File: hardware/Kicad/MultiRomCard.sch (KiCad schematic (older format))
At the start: 9 parts, among them P1 VC4000_Cartridge_Bus, U1 Arduino_UNO, U2 74HC595, U3 74HC595, U4 74HC595, U5 6264, U6 74HC245, U7 74HC245, U8 74HC245

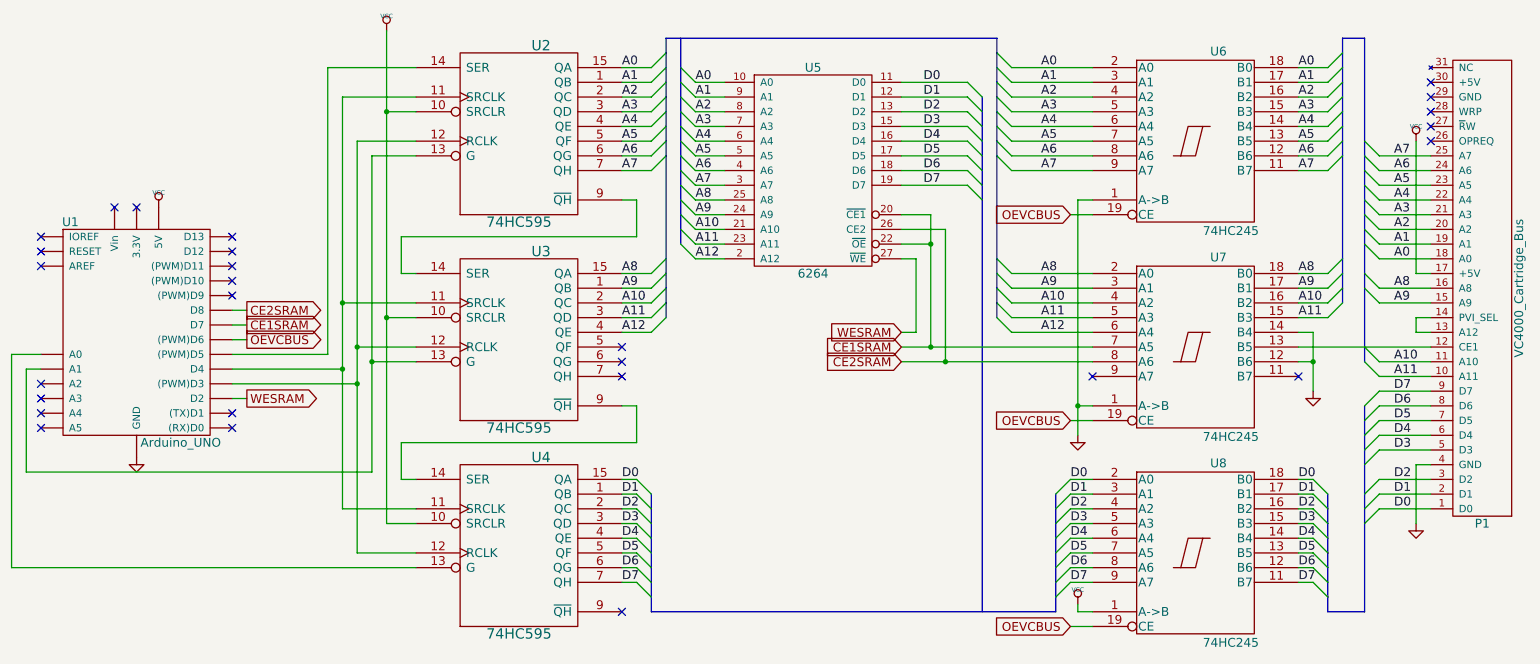
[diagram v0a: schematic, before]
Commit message: Small cosmetic changes in schematic
- Account for changes in Kicad symbol libraries that affected power
  symbols GND and VCC.
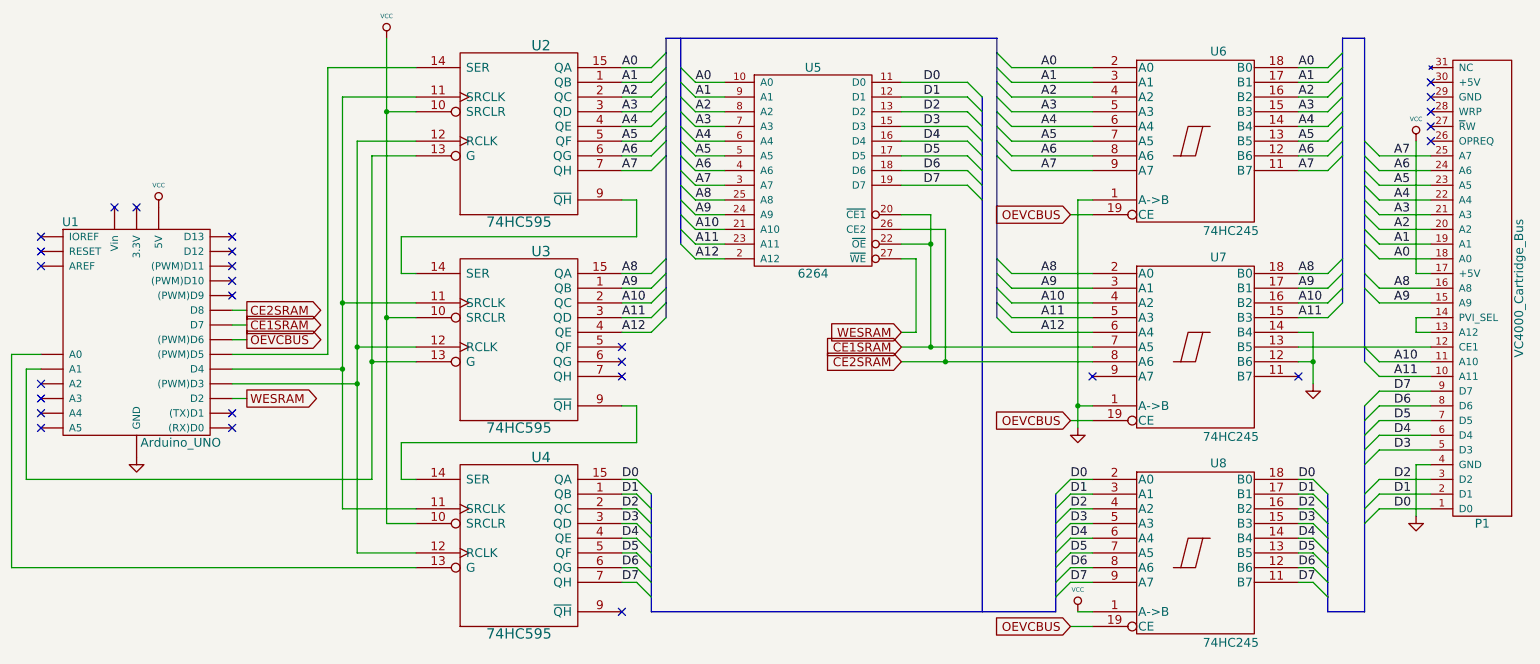
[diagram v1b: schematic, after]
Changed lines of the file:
@@
 P 10250 2350
 F 0 "#PWR7" H 10250 2450 30  0001 C CNN
-F 1 "VCC" H 10250 2450 30  0000 C CNN
+F 1 "VCC" H 10250 2500 30  0000 C CNN
 F 2 "" H 10250 2350 60  0000 C CNN
 F 3 "" H 10250 2350 60  0000 C CNN
@@
 P 1700 2800
 F 0 "#PWR2" H 1700 2900 30  0001 C CNN
-F 1 "VCC" H 1700 2900 30  0000 C CNN
+F 1 "VCC" H 1700 2950 30  0000 C CNN
 F 2 "" H 1700 2800 60  0000 C CNN
 F 3 "" H 1700 2800 60  0000 C CNN
@@
 	1    0    0    -1
 $EndComp
-$Comp
-L GND #PWR1
-U 1 1 54D739DD
-P 1550 4500
-F 0 "#PWR1" H 1550 4500 30  0001 C CNN
-F 1 "GND" H 1550 4430 30  0001 C CNN
-F 2 "" H 1550 4500 60  0000 C CNN
-F 3 "" H 1550 4500 60  0000 C CNN
-	1    1550 4500
-	1    0    0    -1
-$EndComp
 Wire Wire Line
 	4950 3000 3350 3000
@@
 	800  3900 900  3900
 Wire Wire Line
-	3150 4600 800  4600
+	3150 4650 800  4650
 Wire Wire Line
 	3150 2450 3150 3850
 Wire Wire Line
-	3150 3850 3150 4600
+	3150 3850 3150 4650
 Wire Wire Line
 	3150 3850 3450 3850
@@
 Connection ~ 3150 3850
 Wire Wire Line
-	800  4600 800  3900
+	800  4650 800  3900
 Wire Wire Line
 	2950 3900 2200 3900
@@
 L VCC #PWR3
 U 1 1 54DB48BB
-P 3250 1600
-F 0 "#PWR3" H 3250 1700 30  0001 C CNN
-F 1 "VCC" H 3250 1700 30  0000 C CNN
-F 2 "" H 3250 1600 60  0000 C CNN
-F 3 "" H 3250 1600 60  0000 C CNN
-	1    3250 1600
-	1    0    0    -1
-$EndComp
-Wire Wire Line
-	3250 1600 3250 2150
+P 3250 1650
+F 0 "#PWR3" H 3250 1750 30  0001 C CNN
+F 1 "VCC" H 3250 1800 30  0000 C CNN
+F 2 "" H 3250 1650 60  0000 C CNN
+F 3 "" H 3250 1650 60  0000 C CNN
+	1    3250 1650
+	1    0    0    -1
+$EndComp
+Wire Wire Line
+	3250 1650 3250 2150
 Wire Wire Line
 	3250 2150 3250 3550
@@
 L GND #PWR5
 U 1 1 54DB55F6
-P 7950 4350
-F 0 "#PWR5" H 7950 4350 30  0001 C CNN
-F 1 "GND" H 7950 4280 30  0001 C CNN
-F 2 "" H 7950 4350 60  0000 C CNN
-F 3 "" H 7950 4350 60  0000 C CNN
-	1    7950 4350
+P 7950 4300
+F 0 "#PWR5" H 7950 4300 30  0001 C CNN
+F 1 "GND" H 7950 4230 30  0001 C CNN
+F 2 "" H 7950 4300 60  0000 C CNN
+F 3 "" H 7950 4300 60  0000 C CNN
+	1    7950 4300
 	1    0    0    -1
 $EndComp
@@
 L VCC #PWR4
 U 1 1 54DB5800
-P 7950 5500
-F 0 "#PWR4" H 7950 5600 30  0001 C CNN
-F 1 "VCC" H 7950 5600 30  0000 C CNN
-F 2 "" H 7950 5500 60  0000 C CNN
-F 3 "" H 7950 5500 60  0000 C CNN
-	1    7950 5500
+P 7950 5550
+F 0 "#PWR4" H 7950 5650 30  0001 C CNN
+F 1 "VCC" H 7950 5700 30  0000 C CNN
+F 2 "" H 7950 5550 60  0000 C CNN
+F 3 "" H 7950 5550 60  0000 C CNN
+	1    7950 5550
 	1    0    0    -1
 $EndComp
@@
 L GND #PWR8
 U 1 1 54DB7B7A
-P 10250 4950
-F 0 "#PWR8" H 10250 4950 30  0001 C CNN
-F 1 "GND" H 10250 4880 30  0001 C CNN
-F 2 "" H 10250 4950 60  0000 C CNN
-F 3 "" H 10250 4950 60  0000 C CNN
-	1    10250 4950
-	1    0    0    -1
-$EndComp
-Wire Wire Line
-	10250 4950 10250 4550
+P 10250 4900
+F 0 "#PWR8" H 10250 4900 30  0001 C CNN
+F 1 "GND" H 10250 4830 30  0001 C CNN
+F 2 "" H 10250 4900 60  0000 C CNN
+F 3 "" H 10250 4900 60  0000 C CNN
+	1    10250 4900
+	1    0    0    -1
+$EndComp
+Wire Wire Line
+	10250 4900 10250 4550
 Wire Wire Line
 	10250 4550 10350 4550
@@
 L GND #PWR6
 U 1 1 54DB8BDD
-P 9550 4050
-F 0 "#PWR6" H 9550 4050 30  0001 C CNN
-F 1 "GND" H 9550 3980 30  0001 C CNN
-F 2 "" H 9550 4050 60  0000 C CNN
-F 3 "" H 9550 4050 60  0000 C CNN
-	1    9550 4050
+P 9550 4000
+F 0 "#PWR6" H 9550 4000 30  0001 C CNN
+F 1 "GND" H 9550 3930 30  0001 C CNN
+F 2 "" H 9550 4000 60  0000 C CNN
+F 3 "" H 9550 4000 60  0000 C CNN
+	1    9550 4000
 	1    0    0    -1
 $EndComp
@@
 	9550 3650 9550 3850
 Wire Wire Line
-	9550 3850 9550 4050
+	9550 3850 9550 4000
 Wire Wire Line
 	9550 3850 9450 3850
@@
 Wire Bus Line
 	5050 5550 7800 5550
-Wire Wire Line
-	7950 5550 7950 5500
 Connection ~ 7950 4150
 Wire Wire Line
 	7950 2750 7950 4150
 Wire Wire Line
-	7950 4150 7950 4350
+	7950 4150 7950 4300
+$Comp
+L GND #PWR1
+U 1 1 54D739DD
+P 1550 4500
+F 0 "#PWR1" H 1550 4500 30  0001 C CNN
+F 1 "GND" H 1550 4430 30  0001 C CNN
+F 2 "" H 1550 4500 60  0000 C CNN
+F 3 "" H 1550 4500 60  0000 C CNN
+	1    1550 4500
+	1    0    0    -1
+$EndComp
 $EndSCHEMATC

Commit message: Make most pin properties of VC4000_Cartridge_Bus passive to silence Eeschema DRC.
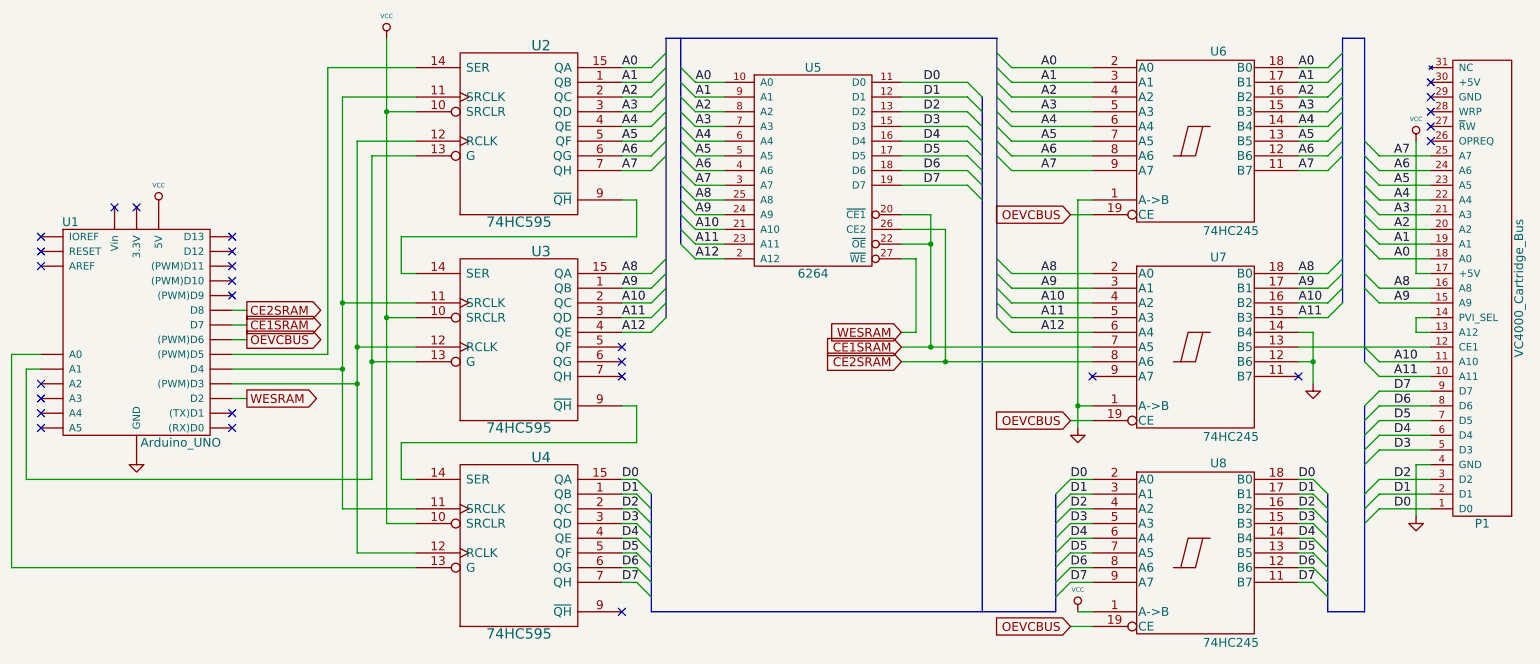
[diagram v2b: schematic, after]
